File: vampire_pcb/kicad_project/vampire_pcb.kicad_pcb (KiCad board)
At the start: 2 copper layers, 66.5 x 14.5 mm, 4 parts, among them J1 VAMPIRE_EDGE, J2 GND_PAD, J3 Conn_01x08, J4 Conn_01x08

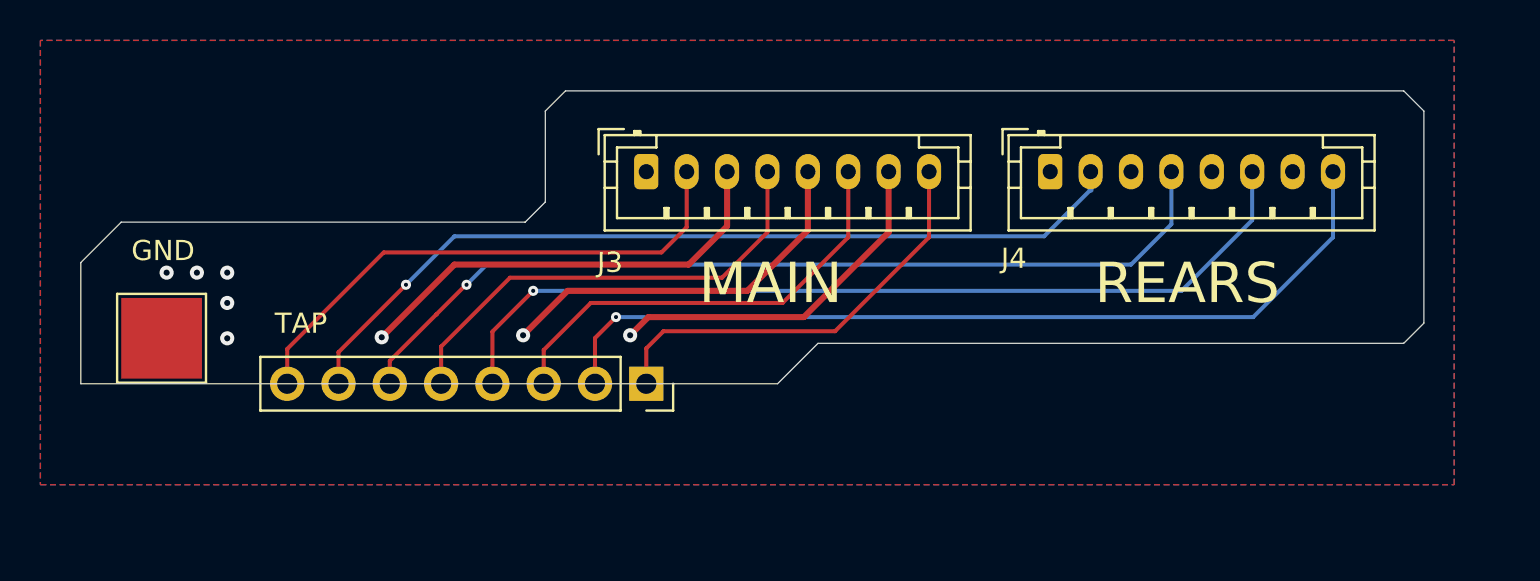
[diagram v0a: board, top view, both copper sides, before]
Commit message: vampire_pcb: use copper pour for GND on front
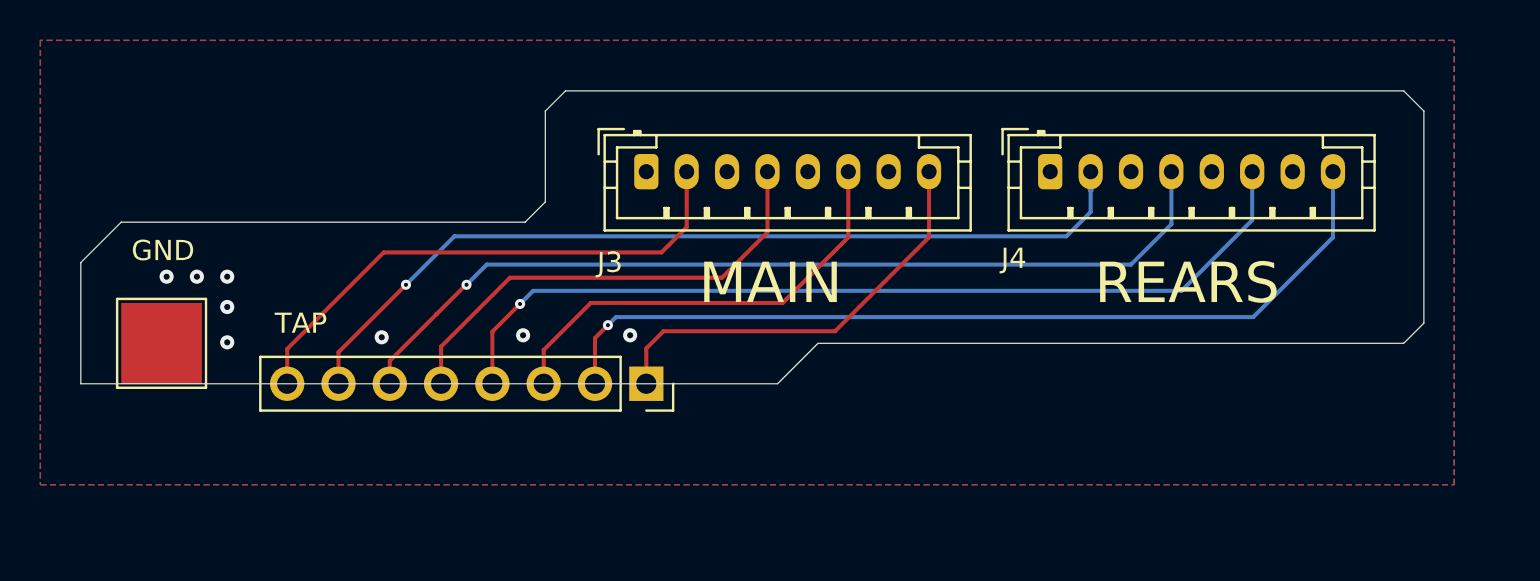
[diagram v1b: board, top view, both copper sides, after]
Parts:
- moved J2 0.25 mm to (94.0, 63.0)
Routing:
- net GND: track 59.1 -> 0.00 mm
- net SBL: track 42.4 -> 43.1 mm
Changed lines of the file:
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@@
 	(footprint "TestPoint:TestPoint_Pad_4.0x4.0mm"
 		(layer "F.Cu")
-		(at 94 62.75 90)
+		(at 94 63 90)
 		(descr "SMD rectangular pad as test Point, square 4.0mm side length")
 		(tags "test point SMD pad rectangle square")
@@
 	)
 	(segment
+		(start 108.5 57.7)
+		(end 138.8 57.7)
+		(width 0.2)
+		(layer "B.Cu")
+		(net 1)
+	)
+	(segment
+		(start 140 56.5)
+		(end 140 55.4)
+		(width 0.2)
+		(layer "B.Cu")
+		(net 1)
+	)
+	(segment
 		(start 106.1 60.1)
 		(end 108.5 57.7)
@@
 	)
 	(segment
-		(start 137.7 57.7)
-		(end 140 55.4)
+		(start 138.8 57.7)
+		(end 140 56.5)
 		(width 0.2)
 		(layer "B.Cu")
 		(net 1)
-	)
-	(segment
-		(start 108.5 57.7)
-		(end 137.7 57.7)
-		(width 0.2)
-		(layer "B.Cu")
-		(net 1)
-	)
-	(segment
-		(start 116.5 61.7)
-		(end 115.46 62.74)
-		(width 0.2)
-		(layer "F.Cu")
-		(net 2)
 	)
 	(segment
@@
 		(net 2)
 	)
-	(via
-		(at 116.5 61.7)
+	(segment
+		(start 116.1 62.1)
+		(end 115.46 62.74)
+		(width 0.2)
+		(layer "F.Cu")
+		(net 2)
+	)
+	(via
+		(at 116.1 62.1)
 		(size 0.5)
 		(drill 0.2)
@@
 	)
 	(segment
+		(start 152 57.75)
+		(end 152 54.5)
+		(width 0.2)
+		(layer "B.Cu")
+		(net 2)
+	)
+	(segment
 		(start 116.5 61.7)
 		(end 148.05 61.7)
@@
 	)
 	(segment
+		(start 116.1 62.1)
+		(end 116.5 61.7)
+		(width 0.2)
+		(layer "B.Cu")
+		(net 2)
+	)
+	(segment
 		(start 148.05 61.7)
 		(end 152 57.75)
-		(width 0.2)
-		(layer "B.Cu")
-		(net 2)
-	)
-	(segment
-		(start 152 57.75)
-		(end 152 54.5)
 		(width 0.2)
 		(layer "B.Cu")
@@
 	)
 	(segment
-		(start 112.4 60.4)
-		(end 110.38 62.42)
-		(width 0.2)
-		(layer "F.Cu")
-		(net 5)
-	)
-	(segment
 		(start 110.38 62.42)
 		(end 110.38 64.4)
@@
 		(net 5)
 	)
-	(via
-		(at 112.4 60.4)
+	(segment
+		(start 111.75 61.05)
+		(end 110.38 62.42)
+		(width 0.2)
+		(layer "F.Cu")
+		(net 5)
+	)
+	(via
+		(at 111.75 61.05)
 		(size 0.5)
 		(drill 0.2)
@@
 	)
 	(segment
+		(start 148 56.9)
+		(end 148 54.5)
+		(width 0.2)
+		(layer "B.Cu")
+		(net 5)
+	)
+	(segment
 		(start 112.4 60.4)
 		(end 144.5 60.4)
@@
 	)
 	(segment
-		(start 148 56.9)
-		(end 148 54.5)
+		(start 111.75 61.05)
+		(end 112.4 60.4)
 		(width 0.2)
 		(layer "B.Cu")
@@
 		(layer "F.Cu")
 		(net 8)
-	)
-	(segment
-		(start 120.1 59.1)
-		(end 108.5 59.1)
-		(width 0.3)
-		(layer "F.Cu")
-		(net 9)
-	)
-	(segment
-		(start 117.2 62.6)
-		(end 118.1 61.7)
-		(width 0.3)
-		(layer "F.Cu")
-		(net 9)
-	)
-	(segment
-		(start 122 57.2)
-		(end 120.1 59.1)
-		(width 0.3)
-		(layer "F.Cu")
-		(net 9)
-	)
-	(segment
-		(start 118.1 61.7)
-		(end 125.8 61.7)
-		(width 0.3)
-		(layer "F.Cu")
-		(net 9)
-	)
-	(segment
-		(start 108.5 59.1)
-		(end 104.9 62.7)
-		(width 0.3)
-		(layer "F.Cu")
-		(net 9)
-	)
-	(segment
-		(start 123 60.4)
-		(end 126 57.4)
-		(width 0.3)
-		(layer "F.Cu")
-		(net 9)
-	)
-	(segment
-		(start 114.1 60.4)
-		(end 123 60.4)
-		(width 0.3)
-		(layer "F.Cu")
-		(net 9)
-	)
-	(segment
-		(start 125.8 61.7)
-		(end 130 57.5)
-		(width 0.3)
-		(layer "F.Cu")
-		(net 9)
-	)
-	(segment
-		(start 126 57.4)
-		(end 126 54.5)
-		(width 0.3)
-		(layer "F.Cu")
-		(net 9)
-	)
-	(segment
-		(start 130 57.5)
-		(end 130 54.5)
-		(width 0.3)
-		(layer "F.Cu")
-		(net 9)
-	)
-	(segment
-		(start 111.9 62.6)
-		(end 114.1 60.4)
-		(width 0.3)
-		(layer "F.Cu")
-		(net 9)
-	)
-	(segment
-		(start 122 54.5)
-		(end 122 57.2)
-		(width 0.3)
-		(layer "F.Cu")
-		(net 9)
 	)
 	(via
@@
 	)
 	(via
-		(at 94.25 59.5)
+		(at 94.25 59.7)
 		(size 0.7)
 		(drill 0.3)
@@
 	)
 	(via
-		(at 97.25 59.5)
+		(at 97.25 59.7)
 		(size 0.7)
 		(drill 0.3)
@@
 	)
 	(via
-		(at 97.25 62.75)
+		(at 97.25 62.95)
 		(size 0.7)
 		(drill 0.3)
@@
 	)
 	(via
-		(at 95.75 59.5)
+		(at 95.75 59.7)
 		(size 0.7)
 		(drill 0.3)
@@
 	)
 	(via
-		(at 97.25 61)
+		(at 97.25 61.2)
 		(size 0.7)
 		(drill 0.3)
@@
 		(polygon
 			(pts
-				(xy 100.3 65) (xy 100.3 63.1) (xy 105 58.4) (xy 118.7 58.5) (xy 120.1 57.1) (xy 120.1 54.5) (xy 132 54.5)
-				(xy 132 57.7) (xy 127.4 62.4) (xy 118.9 62.4) (xy 118 65)
+				(xy 137 53.5) (xy 137.5 53) (xy 152.5 53) (xy 153 53.5) (xy 153 55.5) (xy 152.5 56) (xy 137.5 56)
+				(xy 137 55.5)
 			)
 		)
@@
 		(polygon
 			(pts
-				(xy 137 53.5) (xy 137.5 53) (xy 152.5 53) (xy 153 53.5) (xy 153 55.5) (xy 152.5 56) (xy 137.5 56)
-				(xy 137 55.5)
+				(xy 119.5 53) (xy 119 53.45) (xy 119 54.8) (xy 133.5 54.8) (xy 133.5 53.5) (xy 133 53)
 			)
 		)
@@
 		(net 0)
 		(net_name "")
-		(layers "F&B.Cu")
+		(layer "B.Cu")
 		(hatch edge 0.5)
 		(connect_pads
@@
 		(polygon
 			(pts
-				(xy 119 53.5) (xy 119.5 53) (xy 132.5 53) (xy 133 53.5) (xy 133 55.5) (xy 132.5 56) (xy 119.5 56)
-				(xy 119 55.5)
+				(xy 137.5 53) (xy 137 53.5) (xy 137 54.8) (xy 153 54.8) (xy 153 53.5) (xy 152.5 53)
 			)
 		)
@@
 		(polygon
 			(pts
-				(xy 137.5 53) (xy 137 53.5) (xy 137 54.8) (xy 153 54.8) (xy 153 53.5) (xy 152.5 53)
-			)
-		)
+				(xy 119 53.5) (xy 119.5 53) (xy 132.5 53) (xy 133 53.5) (xy 133 55.5) (xy 132.5 56) (xy 119.5 56)
+				(xy 119 55.5)
+			)
+		)

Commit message: Update PCB
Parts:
- removed J4: Conn_01x08, Connector_JST:JST_PH_B8B-PH-K_1x08_P2.00mm_Vertical
- moved J1 21.5 mm to (139.5, 54.5)
- renumbered J3 to J1, J1 to J2, J2 to J3
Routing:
- net SBR: track 44.7 -> 0.00 mm, vias 1 -> 0
- net SL: track 44.3 -> 0.00 mm, vias 1 -> 0
- net SR: track 43.5 -> 0.00 mm, vias 1 -> 0
- net SBL: track 43.1 -> 0.00 mm, vias 1 -> 0
- net FR: track 20.7 -> 42.2 mm
- net FL: track 22.7 -> 44.3 mm
- net CEN: track 21.7 -> 43.2 mm
- net 12V: track 26.1 -> 47.7 mm
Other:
- board size 66.5 x 14.5 mm -> 68.5 x 22.2 mm
- board text added: "1.AGND 2.12V 3.AGND 4.FL 5.AGND 6.CEN 7.AGND 8.FR"
- board text added: "JLCJLCJLCJLC"
- board text removed: "REARS"
